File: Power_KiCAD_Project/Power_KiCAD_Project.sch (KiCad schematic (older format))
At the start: 55 parts

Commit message: Schematic v.1.0.1
Added XT60 and LiPo Pack Monitor Connectors to schematic file.
Added Temperature Sensor Chips to I2C bus.
Still need to add LiPo Charge Controller chip and DC barrel jack.
Might want to pick slightly larger MCU for 2nd I2C bus, right now sensors are on the main system bus.
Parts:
- removed BT? (x5): Battery_Cell, symbol Device:Battery_Cell
- added J?: XT60, 1X02, symbol SparkFun-Connectors:CONN_02
- added J?: CONN_03X2FEMALE, 2X3, symbol SparkFun-Connectors:CONN_03X2FEMALE
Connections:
- net labels added: PACK_M0, PACK_M1, PACK_M2, PACK_M3, PACK_M4, PACK_M5
- wire segments 169 -> 158
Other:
- note added: "+"
- note added: "-"
- note added: "Battery Pack Connectors"
- note added: "Cell 1"
- note added: "Cell 2"
- note added: "Cell 3"
- note added: "Cell 4"
- note added: "Cell 5"
- moved on the sheet: C?, D?, J?, R?, U?, Y?

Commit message: Schematic v1.0.2
Added Pack+/- tags to LiPo Monitor
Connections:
- net PACK- is gone; now on net GND: J?.1
- net PACK_M5 is gone; now on net PACK+: J?.6, R?.1
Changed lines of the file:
@@
 Title "Power Supply PCB Schematic"
 Date "2021-10-01"
-Rev "v1.0.1"
+Rev "v1.0.2"
 Comp "Missouri S&T Rocket Design Team '21 (Thomas Francois)"
 Comment1 "https://github.com/MSTRocketDesignTeam/Avionics-Power-PCB"
@@
 	1    0    0    -1
 $EndComp
-Wire Wire Line
-	4750 3800 4150 3800
 Wire Wire Line
 	5400 2900 5400 2800
@@
 Connection ~ 4150 3800
 Wire Wire Line
-	4150 3800 4150 4200
+	4150 3800 4150 3950
 Text Notes 3650 4600 0    50   ~ 0
 Simplified Schematic given from BQ76920 datasheet.
@@
 Wire Wire Line
 	4050 2000 4750 2000
-Wire Wire Line
-	4050 1600 4750 1600
 Wire Notes Line
 	4150 1650 4500 1650
@@
 Wire Wire Line
 	7850 1150 8950 1150
+Text GLabel 4050 1450 0    50   Input ~ 0
+PACK+
+Wire Wire Line
+	5400 1500 5400 1600
+Text GLabel 4050 3950 0    50   Input ~ 0
+PACK-
+Wire Wire Line
+	4050 1600 4150 1600
+Wire Wire Line
+	4050 1450 4150 1450
+Wire Wire Line
+	4150 1450 4150 1600
+Connection ~ 4150 1600
+Wire Wire Line
+	4050 3950 4150 3950
+Connection ~ 4150 3950
+Wire Wire Line
+	4150 3950 4150 4200
+Wire Wire Line
+	4150 3800 4750 3800
+Wire Wire Line
+	4150 1600 4750 1600
 $EndSCHEMATC

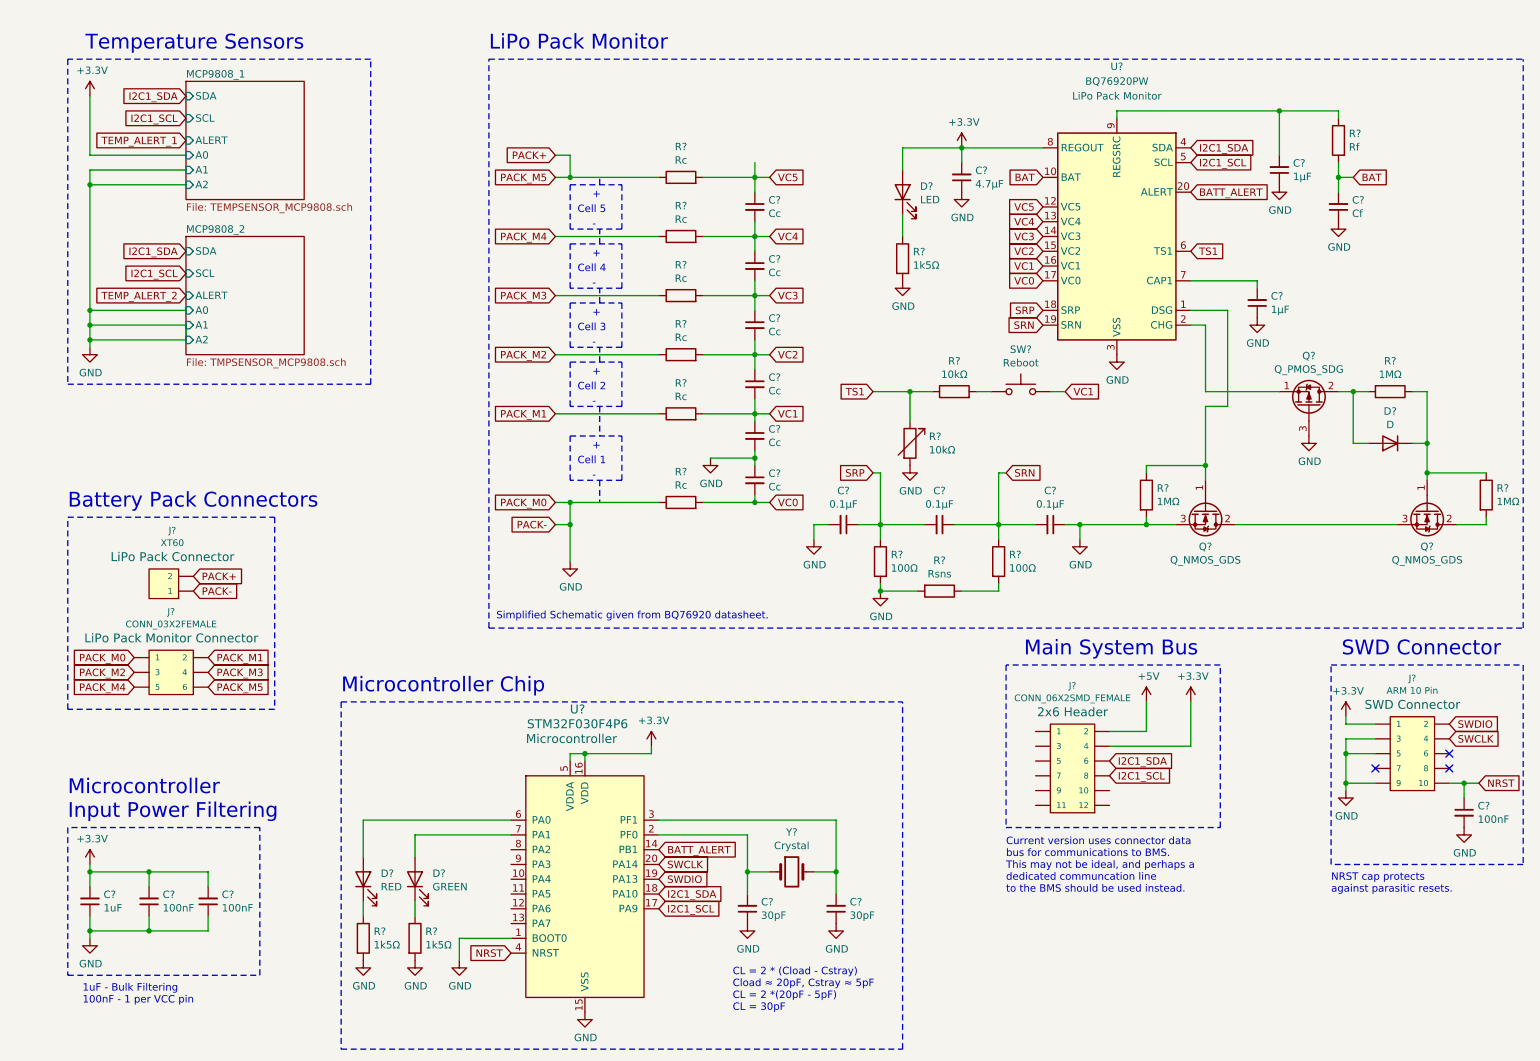
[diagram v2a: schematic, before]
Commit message: Schematic v1.0.3
Compartmentalized the root page.
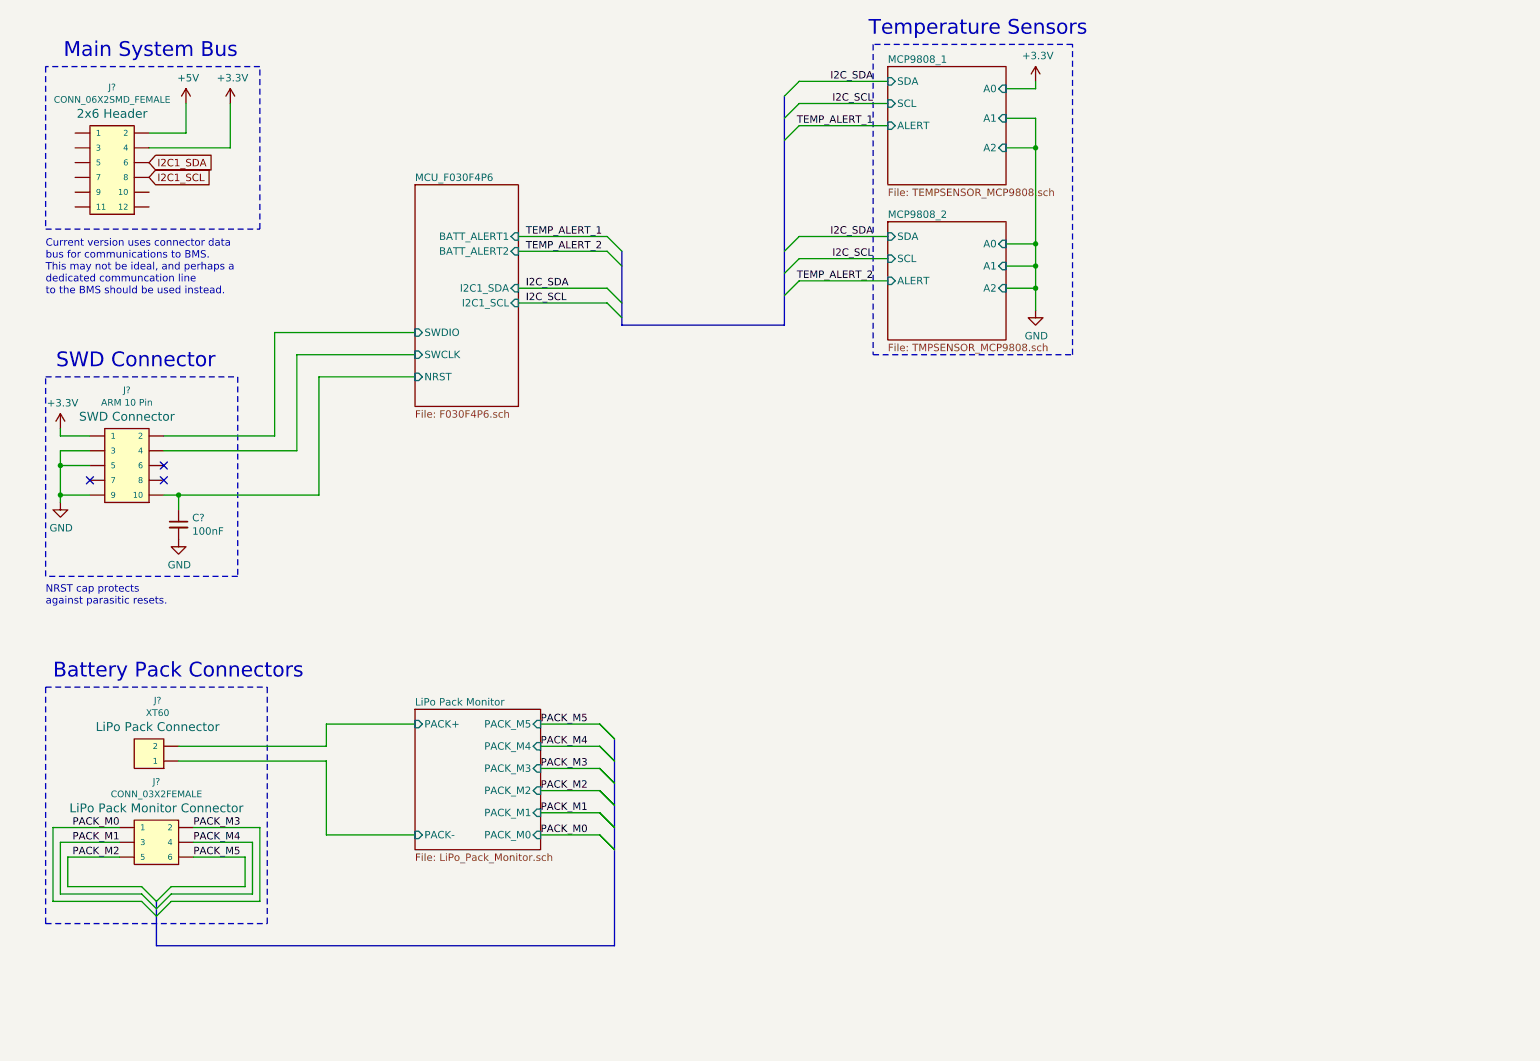
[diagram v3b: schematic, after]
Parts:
- removed C? (x6): Cc, symbol Device:C_Small
- removed C? (x3): 0.1μF, symbol Device:C_Small
- removed C? (x2): 1μF, symbol Device:C_Small
- removed C?: Cf, symbol Device:C_Small
- removed C?: 4.7μF, symbol Device:C_Small
- removed C? (x2): 30pF, symbol Device:C_Small
- removed C?: 1uF, symbol Device:C_Small
- removed C? (x2): 100nF, symbol Device:C_Small
- removed D?: D, symbol Device:D
- removed D?: GREEN, symbol Device:LED
- removed D?: LED, symbol Device:LED
- removed D?: RED, symbol Device:LED
- removed Q? (x2): Q_NMOS_GDS, symbol Device:Q_NMOS_GDS
- removed Q?: Q_PMOS_SDG, symbol Device:Q_PMOS_SDG
- removed R? (x6): Rc, symbol Device:R
- removed R? (x2): 100Ω, symbol Device:R
- removed R?: Rsns, symbol Device:R
- removed R?: 10kΩ, symbol Device:R
- removed R?: 10kΩ, symbol Device:R_Variable
- removed R? (x3): 1MΩ, symbol Device:R
- removed R?: Rf, symbol Device:R
- removed R? (x3): 1k5Ω, symbol Device:R
- removed SW?: Reboot, symbol Switch:SW_Push
- removed U?: BQ76920PW, Package_SO:TSSOP-20_4.4x6.5mm_P0.65mm, symbol Battery_Management:BQ76920PW
- removed U?: STM32F030F4P6, digikey-footprints:TSSOP-20_W4.4mm, symbol dk_Embedded-Microcontrollers:STM32F030F4P6
- removed Y?: Crystal, symbol Device:Crystal
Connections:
- net GND: no longer J?.1, J?.1
- net PACK_M1: now also J?.3; no longer J?.2
- net PACK_M2: now also J?.5; no longer J?.3
- net PACK_M3: now also J?.2; no longer J?.4
- net PACK_M4: now also J?.4; no longer J?.5
- net NRST renamed MCU_F030F4P6/NRST
- net PACK+ renamed LiPo Pack Monitor/PACK+
- net LiPo Pack Monitor/PACK+: no longer J?.6
- net SWCLK renamed MCU_F030F4P6/SWCLK
- net SWDIO renamed MCU_F030F4P6/SWDIO
- new net LiPo Pack Monitor/PACK-: J?.1
- new net PACK_M0: J?.1
- new net PACK_M5: J?.6
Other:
- note removed: "+"
- note removed: "-"
- note removed: "1uF - Bulk Filtering\n100nF - 1 per VCC pin"
- note removed: "CL = 2 * (Cload - Cstray)\nCload ≈ 20pF, Cstray ≈ 5pF\nCL = 2 *(20pF - 5pF)\nCL = 30pF"
- note removed: "Cell 1"
- note removed: "Cell 2"
- note removed: "Cell 3"
- note removed: "Cell 4"
- note removed: "Cell 5"
- note removed: "LiPo Pack Monitor"
- note removed: "Microcontroller Chip"
- note removed: "Microcontroller\nInput Power Filtering"
- note removed: "Simplified Schematic given from BQ76920 datasheet."
- moved on the sheet: C?, J?
